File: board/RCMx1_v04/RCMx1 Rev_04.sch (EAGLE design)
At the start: 72 parts, among them J1 CON_2X2_0_100, J12 CON2X2, J14 CON2X2, J15 CON2X2, J16 CON1X18, J2 CON_2X2_0_100, J20 CON_3X17_0_100, J3 CON_2X16_0_100, J5 M02NG, J6 CON_3X17_0_100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

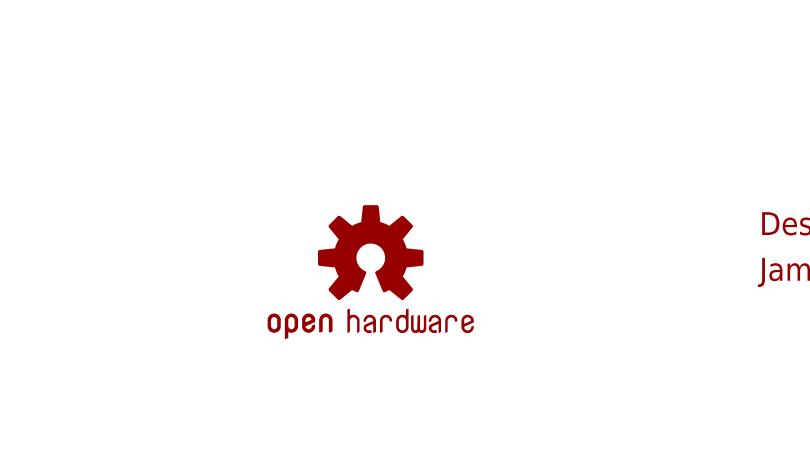
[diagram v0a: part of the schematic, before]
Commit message: Rotated board name on top silk layer 180 degrees.
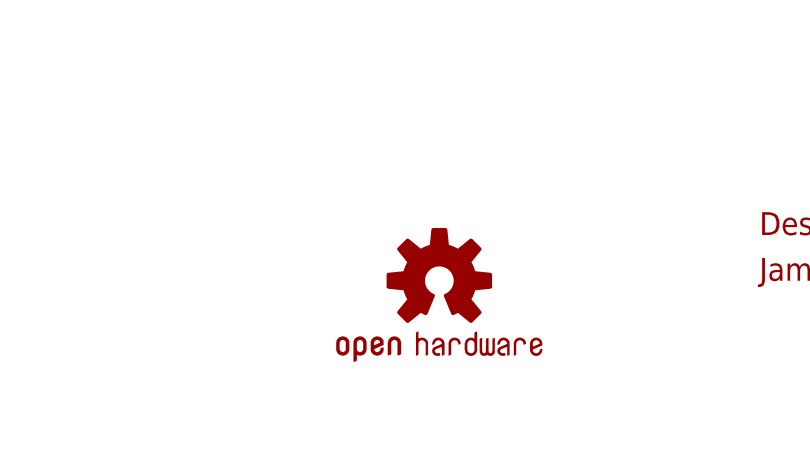
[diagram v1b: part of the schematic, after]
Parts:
- removed LOGO1: OSHW-LOGOM, SparkFun-Aesthetics:OSHW-LOGOM
- added LOGO3: OSHW-LOGOM, SparkFun-Aesthetics:OSHW-LOGOM
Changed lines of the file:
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@@
 <layer number="56" name="wert" color="7" fill="1" visible="no" active="no"/>
 <layer number="57" name="tCAD" color="7" fill="1" visible="no" active="no"/>
+<layer number="59" name="tCarbon" color="7" fill="1" visible="no" active="no"/>
+<layer number="60" name="bCarbon" color="7" fill="1" visible="no" active="no"/>
+<layer number="90" name="Modules" color="5" fill="1" visible="yes" active="yes"/>
 <layer number="91" name="Nets" color="2" fill="1" visible="yes" active="yes"/>
 <layer number="92" name="Busses" color="1" fill="1" visible="yes" active="yes"/>
@@
 <layer number="97" name="Info" color="7" fill="1" visible="yes" active="yes"/>
 <layer number="98" name="Guide" color="6" fill="1" visible="yes" active="yes"/>
+<layer number="99" name="SpiceOrder" color="7" fill="1" visible="no" active="no"/>
 <layer number="100" name="Muster" color="7" fill="1" visible="no" active="no"/>
 <layer number="101" name="Patch_Top" color="12" fill="4" visible="yes" active="yes"/>
@@
 <layer number="111" name="LPC17xx" color="7" fill="1" visible="yes" active="yes"/>
 <layer number="112" name="tSilk" color="7" fill="1" visible="yes" active="yes"/>
+<layer number="113" name="IDFDebug" color="4" fill="1" visible="yes" active="yes"/>
 <layer number="116" name="Patch_BOT" color="9" fill="4" visible="yes" active="yes"/>
 <layer number="121" name="_tsilk" color="7" fill="1" visible="yes" active="yes"/>
@@
 <layer number="127" name="_tValues" color="7" fill="1" visible="yes" active="yes"/>
 <layer number="128" name="_bValues" color="7" fill="1" visible="yes" active="yes"/>
+<layer number="129" name="Mask" color="7" fill="1" visible="yes" active="yes"/>
 <layer number="131" name="tAdjust" color="7" fill="1" visible="no" active="yes"/>
 <layer number="132" name="bAdjust" color="7" fill="1" visible="no" active="yes"/>
@@
 <layer number="223" name="223bmp" color="24" fill="1" visible="no" active="no"/>
 <layer number="224" name="224bmp" color="25" fill="1" visible="no" active="no"/>
+<layer number="225" name="225bmp" color="7" fill="1" visible="yes" active="yes"/>
+<layer number="226" name="226bmp" color="7" fill="1" visible="yes" active="yes"/>
+<layer number="227" name="227bmp" color="7" fill="1" visible="yes" active="yes"/>
+<layer number="228" name="228bmp" color="7" fill="1" visible="yes" active="yes"/>
+<layer number="229" name="229bmp" color="7" fill="1" visible="yes" active="yes"/>
+<layer number="230" name="230bmp" color="7" fill="1" visible="yes" active="yes"/>
+<layer number="231" name="231bmp" color="7" fill="1" visible="yes" active="yes"/>
 <layer number="248" name="Housing" color="7" fill="1" visible="yes" active="yes"/>
 <layer number="249" name="Edge" color="7" fill="1" visible="yes" active="yes"/>
@@
 <layer number="251" name="SMDround" color="12" fill="11" visible="no" active="no"/>
 <layer number="254" name="cooling" color="7" fill="1" visible="yes" active="yes"/>
+<layer number="255" name="routoute" color="7" fill="1" visible="yes" active="yes"/>
 </layers>
 <schematic xreflabel="%F%N/%S.%C%R" xrefpart="/%S.%C%R">
@@
 <part name="FID2" library="adafruit" deviceset="FIDUCIAL" device=""/>
 <part name="FID3" library="adafruit" deviceset="FIDUCIAL" device=""/>
-<part name="LOGO1" library="SparkFun-Aesthetics" deviceset="OSHW-LOGO" device="M"/>
 <part name="U$3" library="SchmalzHausPublic" deviceset="ROHS_GARBAGE" device=""/>
+<part name="LOGO3" library="SparkFun-Aesthetics" deviceset="OSHW-LOGO" device="M"/>
 </parts>
 <sheets>
@@
 <instance part="FID2" gate="G$1" x="342.9" y="-134.62"/>
 <instance part="FID3" gate="G$1" x="350.52" y="-134.62"/>
-<instance part="LOGO1" gate="G$1" x="281.94" y="-152.4"/>
 <instance part="U$3" gate="G$1" x="335.28" y="-142.24"/>
+<instance part="LOGO3" gate="G$1" x="289.56" y="-154.94"/>
 </instances>
 <busses>
